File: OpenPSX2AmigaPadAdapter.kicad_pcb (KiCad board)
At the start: 2 copper layers, 74.5 x 44.2 mm, 33 parts, among them J1 TO_PSX_PAD, J2 TO_AMI, J3 CONN_FTDI, J4 CONN_ICSP, Q1 BSS138, Q2 BSS138, Q3 BSS138, Q4 BSS138, U1 ATmega328P-AU, U2 LM1117-3.3, Y1 16MHz

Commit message: Ready?
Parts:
- added D1: 1n5817, Diode_SMD:D_SMA_Handsoldering, F.Cu at (152.9, 85.6)
- added J99: OSHW_LOGO, Symbol:OSHW-Logo_5.7x6mm_Copper, B.Cu at (139.1, 75.2)
- J2: footprint w_conn_d-sub:DB_9F -> OpenPSX2AmigaPadAdapter:DB_9F
- moved LD1 16.5 mm to (150.1, 68.8), turned to 180 degrees
- moved LD2 16.0 mm to (150.1, 65.0), turned to 180 degrees
- moved R2 15.5 mm to (131.2, 80.3)
- moved R5 15.5 mm to (131.2, 64.8)
- moved R6 15.5 mm to (124.2, 80.3)
- moved R9 15.5 mm to (124.2, 64.8)
- moved J4 12.4 mm to (139.7, 69.6), turned to 180 degrees
- moved R11 7.55 mm to (145.0, 68.8), turned to 180 degrees
- moved R12 6.25 mm to (145.0, 65.0), turned to 180 degrees
- moved R3 5.16 mm to (131.2, 75.1)
- moved R4 5.16 mm to (131.2, 69.9)
- moved R7 5.16 mm to (124.2, 75.1)
- moved R8 5.16 mm to (124.2, 69.9)
- moved C3 4.63 mm to (143.6, 84.5), turned to 90 degrees
- moved C5 4.57 mm to (146.8, 70.9)
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- renumbered D1 to LD1, D2 to LD2
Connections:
- J2 pad 7: +5V -> Net-(D1-Pad2)
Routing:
- net +5V: track 28.4 -> 93.6 mm, vias 1 -> 5
- net /ps_attn: track 3.04 -> 50.8 mm, vias 0 -> 1
- net /miso: track 16.2 -> 55.5 mm, vias 0 -> 1
- net /ps_clk: track 12.7 -> 48.4 mm
- net +3V3: track 21.4 -> 53.4 mm, vias 0 -> 4
- net /mosi: track 27.4 -> 55.0 mm, vias 0 -> 1
- net Net-(D1-Pad2): track 0.00 -> 20.4 mm
- net /ps_cmd_3v3: track 2.46 -> 21.6 mm
- net /ps_data_3v3: track 2.52 -> 20.8 mm
- net /ps_clk_3v3: track 2.40 -> 11.9 mm
- net /ps_attn_3v3: track 2.40 -> 11.3 mm
- net /led1: track 11.2 -> 3.97 mm
- net Net-(C6-Pad2): track 11.7 -> 14.7 mm
- net Net-(C7-Pad2): track 9.37 -> 11.4 mm
- net /led2: track 6.47 -> 7.60 mm
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- added copper zone on B.Cu, net GND
- added copper zone on F.Cu, net GND
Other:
- board size 74.5 x 44.2 mm -> 73.7 x 44.2 mm
- rule pad_to_mask_clearance: 0.051 -> 0
- board text added: "+5V"
- board text added: "DTR"
- board text added: "FTDI"
- board text added: "GND"
- board text added: "ICSP"
- board text added: "RX"
- board text added: "TX"
- board text added: "V1"
- board text added: "github.com/SukkoPera/OpenPSX2AmigaPadAdapter"

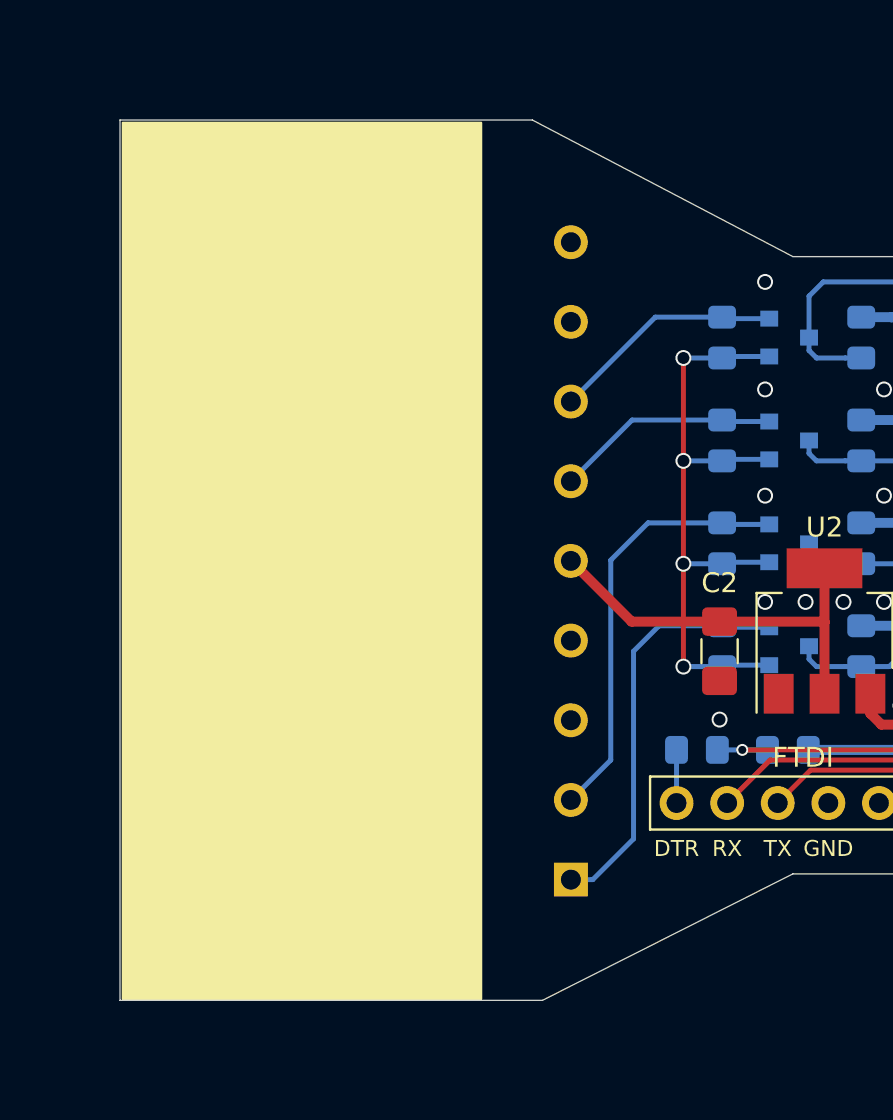
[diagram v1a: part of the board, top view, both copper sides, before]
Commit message: Ready for prototype
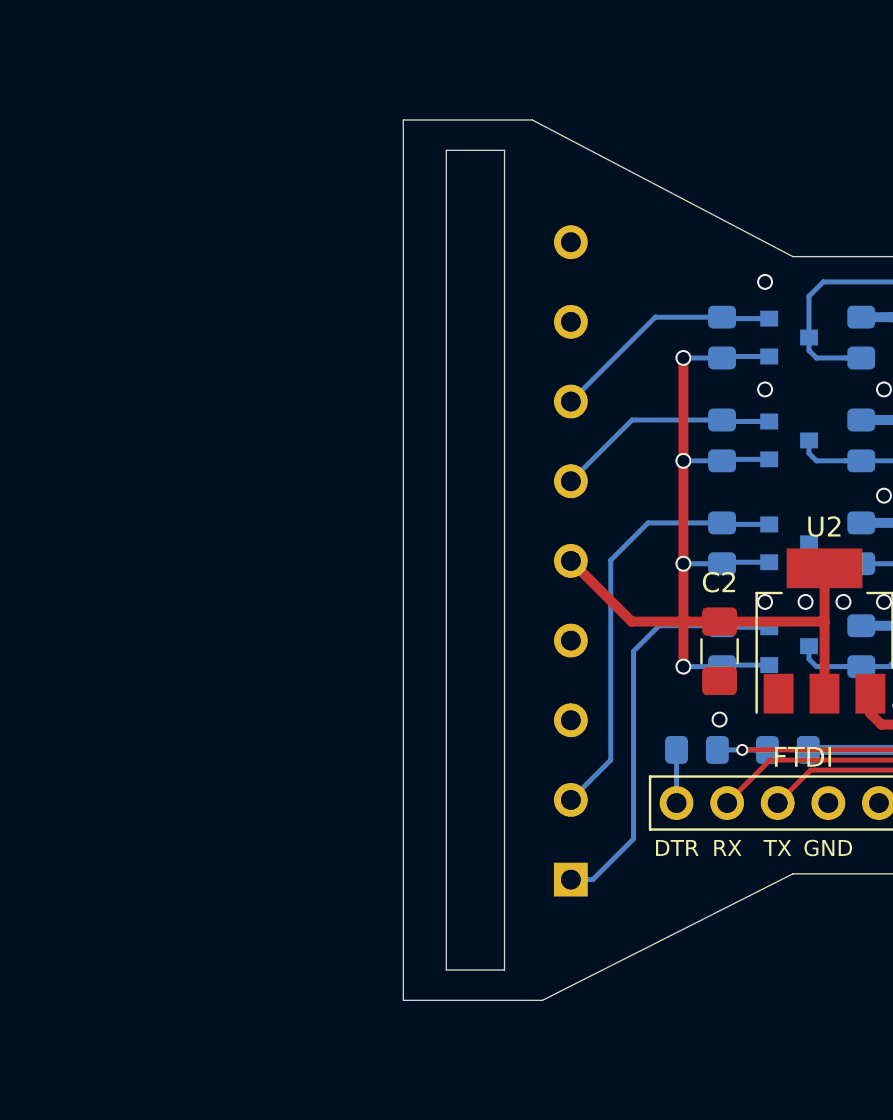
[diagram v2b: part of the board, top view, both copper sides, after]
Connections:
- J1 pad 3: +9V -> (no net)
- J1 pad 8: Net-(J1-Pad8) -> (no net)
- J1 pad 9: /ps_ack_3v3 -> (no net)
- J3 pad 2: Net-(J3-Pad2) -> (no net)
- U1 pad 13: Net-(U1-Pad13) -> (no net)
- U1 pad 19: Net-(U1-Pad19) -> (no net)
- U1 pad 20: Net-(U1-Pad20) -> (no net)
- U1 pad 22: Net-(U1-Pad22) -> (no net)
- U1 pad 25: Net-(U1-Pad25) -> (no net)
- U1 pad 26: Net-(U1-Pad26) -> (no net)
- U1 pad 27: Net-(U1-Pad27) -> (no net)
- U1 pad 28: Net-(U1-Pad28) -> (no net)
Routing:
- net GND: vias 53 -> 38
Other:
- board size 73.7 x 44.2 mm -> 59.4 x 44.2 mm
